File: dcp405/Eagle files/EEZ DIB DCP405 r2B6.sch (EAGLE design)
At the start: 307 parts, among them IC1 LTC3864EMSE#PBF, IC10 MC33272ADR2G, IC11 LTC2050HVCS8#PBF, IC12 74AUP1G74DC.125, IC13 MCP23S17-E/SS, IC14 REF5025AIDR, IC15 TC77-5.0MCTTR, IC16 DAC8552IDGKR, IC17 SN74LVC1G3157DCKR, IC18 ADS1120IPWR, IC19 LM293D, IC2 TPS54060DGQ, IC20 MAX9141ESA, IC3 SI8641BB-B-IS1, IC4 SN74LVC1G139DCUR, IC5 MC78L05, IC6 MC79L05, IC7 SI8641BB-B-IS1, IC8 M24C32-WMN6P, IC9 MC33272ADR2G, J1 4907, J2 FCR7350R, J3 FCR7350B, K1 G6K-2F-5DC, Q1 SUD19P06-60, Q10 PSMN0R9-25YLC, Q11 PSMN0R9-25YLC, Q12 BSS84P, Q13 BTA26-600, Q14 FMMT493TA, Q15 2N7002, Q16 2N7002, Q17 2N7002, Q18 MMBT5551, Q19 MMBT5401, Q2 MMBT5401, Q20 MMBT5551, Q21 MMBT5551, Q22 2N7002, Q3 D45H11FP, Q4 D45H11FP, Q5 FQPF11P06 or FQPF27P06, Q6 BCP56-16.115, Q7 MMBT5401, Q8 NZT605, Q9 BSS205NH6327XTSA1, X1 39-30-1020, X2 77317-104-28LF, X3 1844249, X4 DS1024-2*10R0

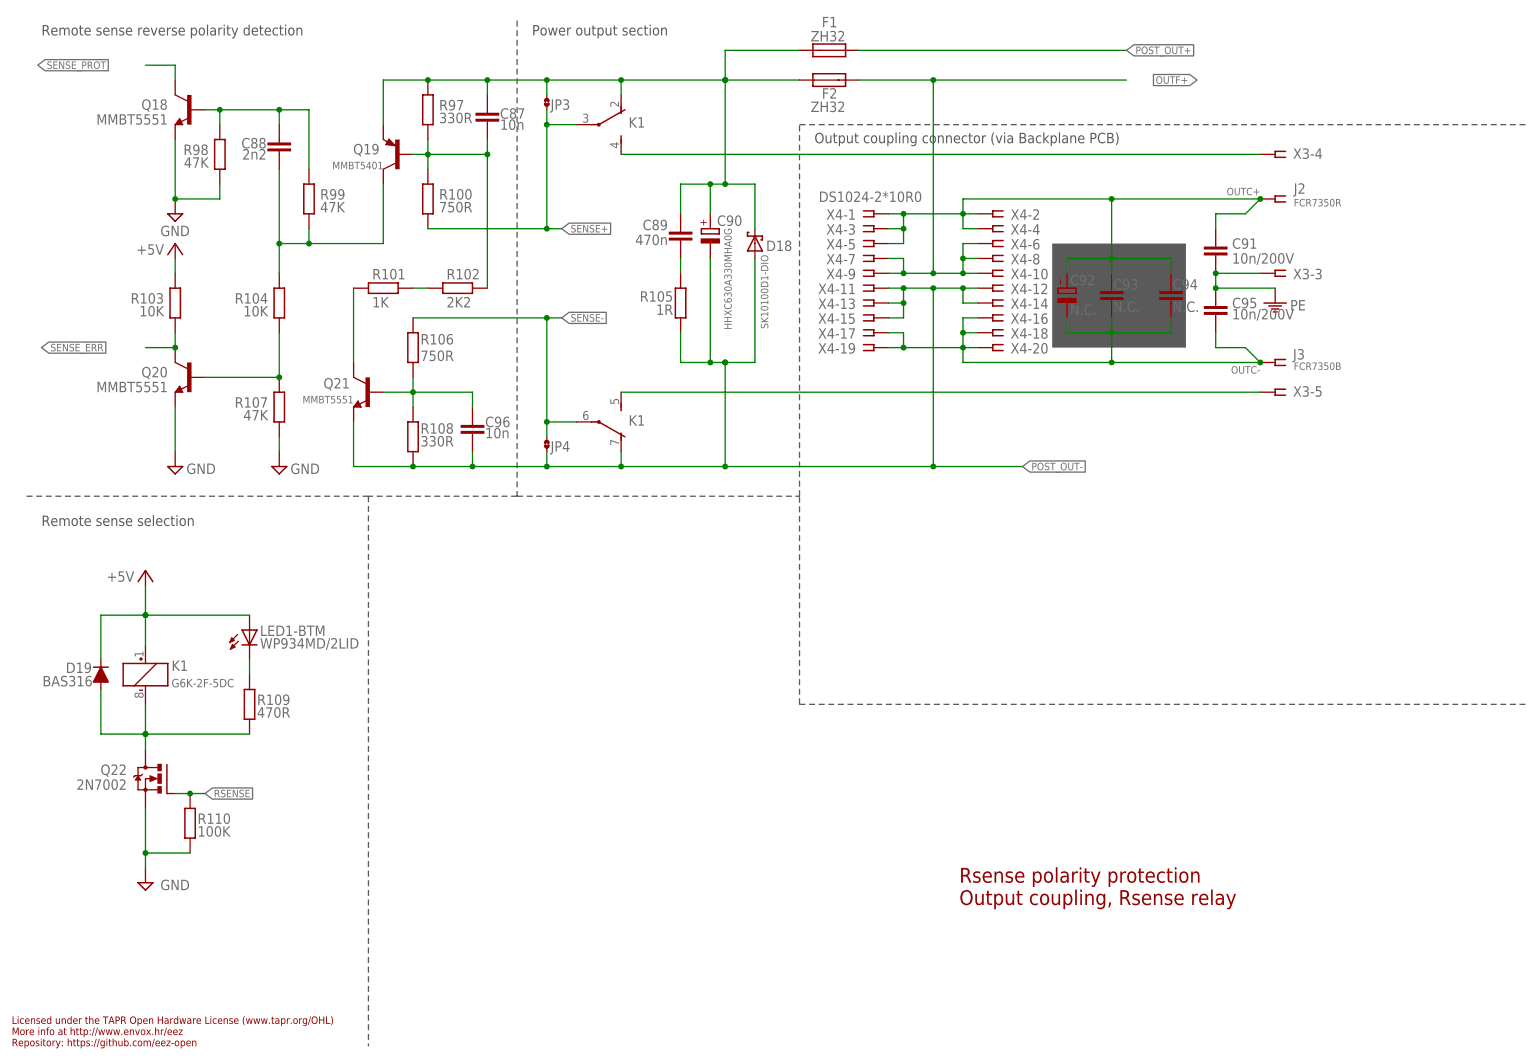
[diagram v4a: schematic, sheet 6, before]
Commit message: DCP405 reverse sense clean up
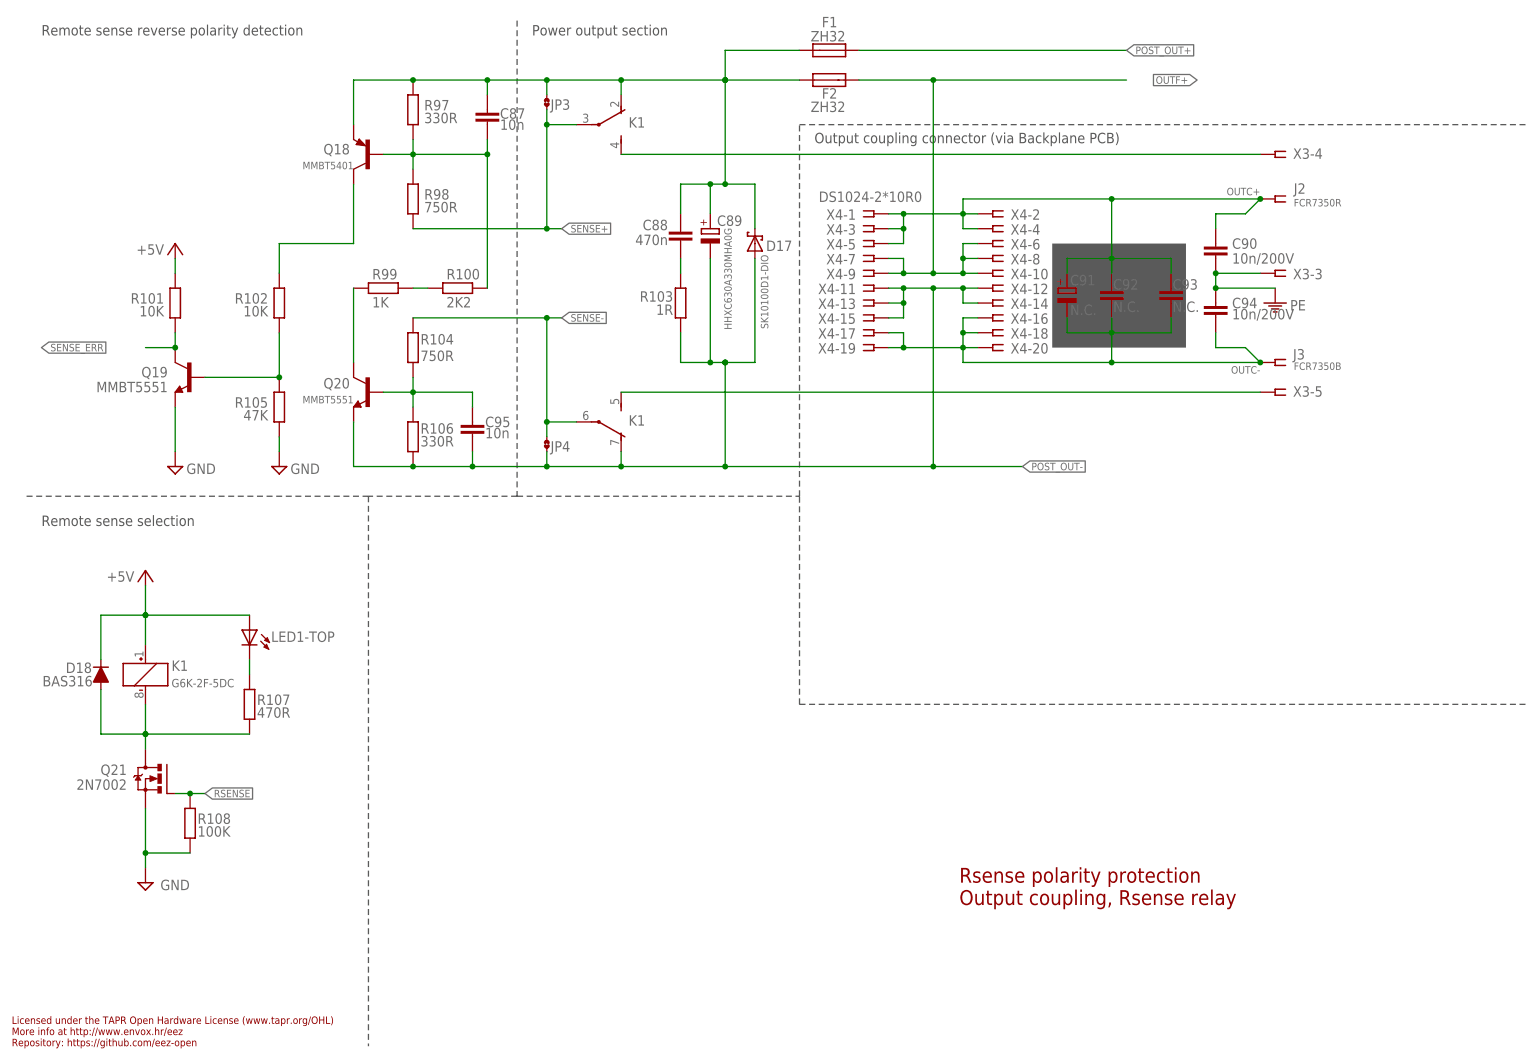
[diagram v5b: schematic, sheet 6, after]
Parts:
- removed C96: 10n, rcl:C-EUC0805
- removed D19: BAS316, EEZ_Lib1:DIODESOD323R
- removed Q22: 2N7002, EEZ_Lib1:2N7002
- removed R109: 470R, rcl:R-EU_R0805
- removed R110: 100K, rcl:R-EU_R0805
- added C27: 4u7, rcl:C-EUC1206
- C2: value HHXC630A330MHA0G -> HHXC630A330MHA0G
- C28: value 4u7 -> 10n; device rcl:C-EUC1206 -> rcl:C-EUC0805
- C29: value 10n -> 18p; device rcl:C-EUC0805 -> rcl:C-EUC0603
- C30: value 18p -> 100n
- C33: value 100n -> 10n; device rcl:C-EUC0603 -> rcl:C-EUC0805
- C34, C47: value 10n -> 100n; device rcl:C-EUC0805 -> rcl:C-EUC0603
- C40: value 100n -> 470p; device rcl:C-EUC0603 -> rcl:C-EUC0805
- C41: value 470p -> 2n2
- C42, C45: value 2n2 -> 33p
- C43: value 33p -> 330p
- C44: value 330p -> 2n2
- C46: value 33p -> 10n
- C50: value 100n -> 1u; device rcl:C-EUC0603 -> rcl:C-EUC0805
- C51: value 1u -> 10n
- C52: value 10n -> 6n8
- C53: value 6n8 -> 1u
- C54: value 1u -> 100n; device rcl:C-EUC0805 -> rcl:C-EUC0603
- C57: value 100n -> 33p; device rcl:C-EUC0603 -> rcl:C-EUC0805
- C88: value 2n2 -> 470n; device rcl:C-EUC0805 -> rcl:C-EUC1206
- C89: value 470n -> HHXC630A330MHA0G; device rcl:C-EUC1206 -> EEZ_Lib1:ECAPSMD8.3MM/HA0
- C90: value HHXC630A330MHA0G -> 10n/200V; device EEZ_Lib1:ECAPSMD8.3MM/HA0 -> rcl:C-EUC1206
- C91: value 10n/200V -> N.C.; device rcl:C-EUC1206 -> EEZ_Lib1:ECAP2G/5
- C92: device EEZ_Lib1:ECAP2G/5 -> rcl:C-EUC0805
- C94: value N.C. -> 10n/200V; device rcl:C-EUC0805 -> rcl:C-EUC1206
- C95: value 10n/200V -> 10n; device rcl:C-EUC1206 -> rcl:C-EUC0805
- D17: value BAS316 -> SK10100D1-DIO; device EEZ_Lib1:DIODESOD323R -> EEZ_Lib1:SCHOTTKY-DUAL_A_L
- D18: value SK10100D1-DIO -> BAS316; device EEZ_Lib1:SCHOTTKY-DUAL_A_L -> EEZ_Lib1:DIODESOD323R
- JP1: value JP2-CUT -> JP2-NOCUT; device EEZ_Lib1:JP2-CUT -> EEZ_Lib1:JP2-NOCUT
- Q18: value MMBT5551 -> MMBT5401; device transistor:MMBT5551LT1-NPN-SOT23-BEC -> transistor:BC857B-PNP-SOT23-BEC
- Q19: value MMBT5401 -> MMBT5551; device transistor:BC857B-PNP-SOT23-BEC -> transistor:MMBT5551LT1-NPN-SOT23-BEC
- Q21: value MMBT5551 -> 2N7002; device transistor:MMBT5551LT1-NPN-SOT23-BEC -> EEZ_Lib1:2N7002; MPN (none) -> 2N7002-7-F; OC_FARNELL (none) -> 1713823; OC_NEWARK (none) -> 25R5679; PACKAGE (none) -> SOT-23-3; SUPPLIER (none) -> DIODES INC.
- R100: value 750R -> 2K2
- R101: value 1K -> 10K
- R102: value 2K2 -> 10K
- R103: value 10K -> 1R
- R104: value 10K -> 750R
- R105: value 1R -> 47K
- R106: value 750R -> 330R
- R107: value 47K -> 470R
- R108: value 330R -> 100K
- R51: value 36K -> 2K2
- R63: value 10K -> 0R010 (low TCR); device rcl:R-EU_R0805 -> EEZ_Lib1:R-EU_4WIRE2512
- R64: value 0R010 (low TCR) -> 2K2; device EEZ_Lib1:R-EU_4WIRE2512 -> rcl:R-EU_R0805
- R98: value 47K -> 750R
- R99: value 47K -> 1K
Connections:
- removed net N$111: C88.1, Q18.B, R98.2, R99.2
- removed net SENSE_PROT: D14.C, Q18.C
- net +3V3: now also C30.1, C35.1, C38.2; no longer C31.1, C36.1, C39.2
- net +5V: now also C31.2, C32.1, C36.2, D18.C, LED1-TOP.A, R101.2; no longer C32.2, C33.1, C37.2, D19.C, LED1-BTM.A, R103.2
- net +5VOUT: now also C34.1; no longer C35.1
- net +VNR: now also C27.1; no longer C28.1
- net 5A_S: now also R63.2; no longer R64.2
- net AUX_USET_SW: now also LED1-BTM.A; no longer LED1-TOP.A
- net GND: now also C27.2, C29.1, C31.1, C32.2, C33.1, C34.2, C36.1, C39.2, C46.1, C47.2, C48.1, C53.1, C54.2, C55.1, D16.C, Q19.E, Q21.S, R105.1, R108.1; no longer C29.2, C30.1, C32.1, C33.2, C34.1, C35.2, C38.1, C40.2, C47.1, C48.2, C52.1, C54.1, C55.2, C57.1, D17.C, Q18.E, Q20.E, Q22.S, R107.1, R110.1, R98.1
- net GNDIO: now also C30.2, C35.2, C38.1; no longer C31.2, C36.2, C39.1
- net ISENSE-: now also C58.1
- net I_MON: now also C58.2
- net I_SERVO: now also C52.2, C57.2; no longer C53.2, C58.2
- net N$102: now also C39.1; no longer C40.1
- net N$107: now also Q18.B, R98.2; no longer Q19.B, R102.2
- net N$108: now also Q18.C, R102.2; no longer C88.2, Q19.C, R104.2, R99.1
- net N$109: now also Q20.C, R99.1; no longer Q21.C, R101.1
- net N$11: now also R63.2S; no longer R64.2S
- net N$110: now also C95.1, Q20.B, R104.1, R106.2; no longer C96.1, Q21.B, R106.1, R108.2
- net N$112: now also Q19.B, R102.1, R105.2; no longer Q20.B, R104.1, R107.2
- net N$113: now also C88.2, R103.2; no longer C89.2, R105.2
- net N$114: now also D18.A, Q21.D, R107.1; no longer D19.A, Q22.D, R109.1
- net N$120: now also LED1-TOP.C, R107.2; no longer LED1-BTM.C, R109.2
- net N$121: now also LED1-BTM.C; no longer LED1-TOP.C
- net N$14: now also C43.1; no longer C44.1
- net N$158: now also C42.1; no longer C43.1
- net N$173: now also R100.1, R99.2; no longer R101.2, R102.1
- net N$20: now also D15.C, D16.A; no longer D16.C, D17.A
- net N$200: now also R63.1S; no longer R64.1S
- net N$21: now also D15.A; no longer D16.A
- net N$29: now also C37.2; no longer C38.2
- net N$37: now also C52.1; no longer C53.1
- net N$41: now also C28.1; no longer C29.1
- net N$45: now also C40.2; no longer C41.2
- net N$50: now also C29.2; no longer C30.2
- net N$51: now also C33.2; no longer C34.2
- net N$55: now also C40.1; no longer C41.1
- net N$56: no longer D15.A
- net N$84: now also C45.1; no longer C46.1
- net N$88: now also R64.1; no longer R63.1
- net N$89: now also C57.1, R64.2; no longer C58.1, R63.2
- net N$90: now also C41.2; no longer C42.2
- net N$91: now also C44.2; no longer C45.2
- net OUTC+: now also C90.1, C91.+, C92.1; no longer C91.1, C92.+, C94.1
- net OUTC-: now also C91.-, C92.2; no longer C92.-, C95.2
- net PE: now also C90.2, C94.1; no longer C91.2, C95.1
- net POST_OUT+: now also C44.1; no longer C45.1
- net POST_OUT-: now also C41.1, C89.-, C95.2, D17.A, Q20.E, R103.1, R106.1; no longer C42.1, C90.-, C96.2, D18.A, Q21.E, R105.1, R108.1
- net POST_OUTF+: now also C88.1, C89.+, D17.C, Q18.E; no longer C89.1, C90.+, D18.C, Q19.E
- net PREG_OUT-: now also R63.1; no longer R64.1
- net PWRGOOD: now also D14.C; no longer D15.C
- net RSENSE: now also Q21.G, R108.2; no longer Q22.G, R110.2
- net SENSE+: now also R98.1; no longer R100.1
- net SENSE-: now also R104.2; no longer R106.2
- net SENSE_ERR: now also Q19.C, R101.1; no longer Q20.C, R103.1
- net U_MON: now also C42.2; no longer C43.2
- net U_SERVO: now also C43.2, C45.2; no longer C44.2, C46.2
- net V+: now also C46.2, C47.1, C48.2; no longer C47.2, C48.1, C51.2
- net V-: now also C51.2, C53.2, C54.1, C55.2; no longer C52.2, C54.2, C55.1, C57.2
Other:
- moved on the sheet: C28, C29, C30, C31, C32, C33, C34, C35, C36, C37, C38, C40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
